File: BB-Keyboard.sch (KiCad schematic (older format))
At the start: 35 parts, among them SW1 SW_Q, SW10 SW_X, SW11 SW_0, SW12 SW_R, SW13 SW_F, SW14 SW_C, SW15 SW_T, SW16 SW_G, SW17 SW_V, SW18 SW_SPC, SW19 SW_Y, SW2 SW_A, SW20 SW_H, SW21 SW_B, SW22 SW_U, SW23 SW_J, SW24 SW_N, SW25 SW_I, SW26 SW_K, SW27 SW_M, SW28 SW_SYM, SW29 SW_O, SW3 SW_ALT, SW30 SW_L, SW31 SW_$, SW32 SW_RSHIFT, SW33 SW_P, SW34 SW_BK, SW35 SW_ENT, SW4 SW_W, SW5 SW_S, SW6 SW_Z, SW7 SW_LSHIFT, SW8 SW_E, SW9 SW_D

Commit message: Buses, labels, et al.
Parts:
- added D? (x35): D, symbol D
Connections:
- new net: D?.1 (K), SW1.2
- new net: D?.1 (K), SW4.2
- new net: D?.1 (K), SW8.2
- new net: D?.1 (K), SW12.2
- new net: D?.1 (K), SW15.2
- new net: D?.1 (K), SW19.2
- new net: D?.1 (K), SW22.2
- new net: D?.1 (K), SW25.2
- new net: D?.1 (K), SW29.2
- new net: D?.1 (K), SW33.2
- new net: D?.1 (K), SW2.2
- new net: D?.1 (K), SW5.2
- new net: D?.1 (K), SW9.2
- new net: D?.1 (K), SW13.2
- new net: D?.1 (K), SW16.2
- new net: D?.1 (K), SW20.2
- new net: D?.1 (K), SW23.2
- new net: D?.1 (K), SW26.2
- new net: D?.1 (K), SW30.2
- new net: D?.1 (K), SW34.2
- new net: D?.1 (K), SW3.2
- new net: D?.1 (K), SW6.2
- new net: D?.1 (K), SW10.2
- new net: D?.1 (K), SW14.2
- new net: D?.1 (K), SW17.2
- new net: D?.1 (K), SW21.2
- new net: D?.1 (K), SW24.2
- new net: D?.1 (K), SW27.2
- new net: D?.1 (K), SW31.2
- new net: D?.1 (K), SW35.2
- new net: D?.1 (K), SW7.2
- new net: D?.1 (K), SW11.2
- new net: D?.1 (K), SW18.1
- new net: D?.1 (K), SW28.2
- new net: D?.1 (K), SW32.2
- new net COL0: D?.2 (A)
- new net COL1: D?.2 (A)
- new net COL2: D?.2 (A)
- new net COL3: D?.2 (A)
- new net COL4: D?.2 (A)
- new net COL5: D?.2 (A)
- new net COL6: D?.2 (A)
- new net COL7: D?.2 (A)
- new net COL8: D?.2 (A)
- new net COL9: D?.2 (A)
- now unconnected: SW1.1, SW10.1, SW11.1, SW12.1, SW13.1, SW14.1, SW15.1, SW16.1, SW17.1, SW18.2, SW19.1, SW2.1, SW20.1, SW21.1, SW22.1, SW23.1, SW24.1, SW25.1, SW26.1, SW27.1, SW28.1, SW29.1, SW3.1, SW30.1, SW31.1, SW32.1, SW33.1, SW34.1, SW35.1, SW4.1, SW5.1, SW6.1, SW7.1, SW8.1, SW9.1
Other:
- moved on the sheet: SW1, SW10, SW11, SW12, SW13, SW14, SW15, SW16, SW17, SW18, SW19, SW2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

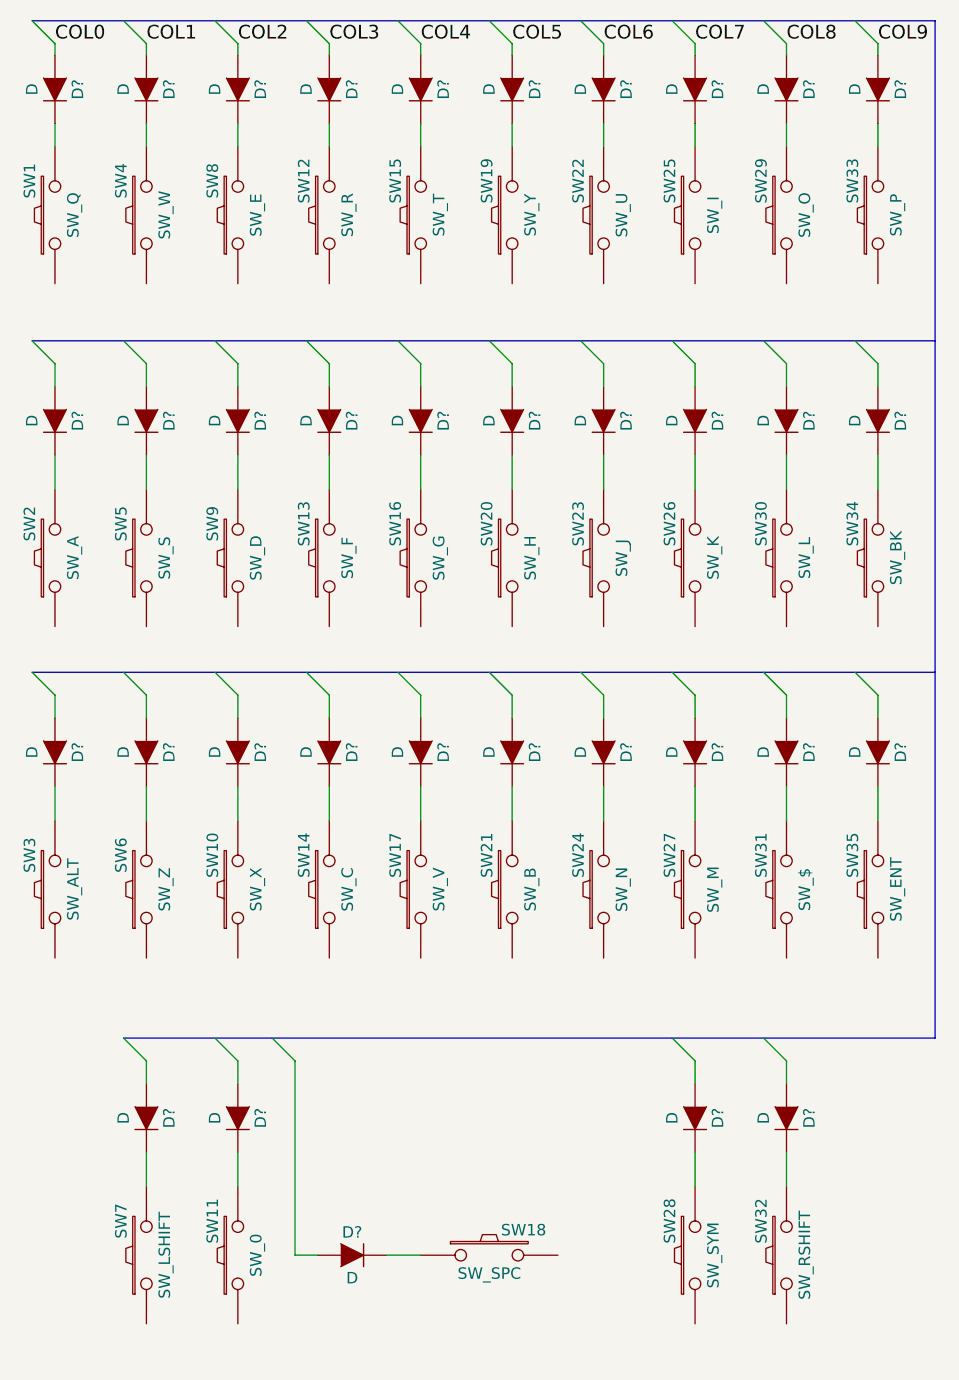
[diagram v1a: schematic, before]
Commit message: More labels and buses.
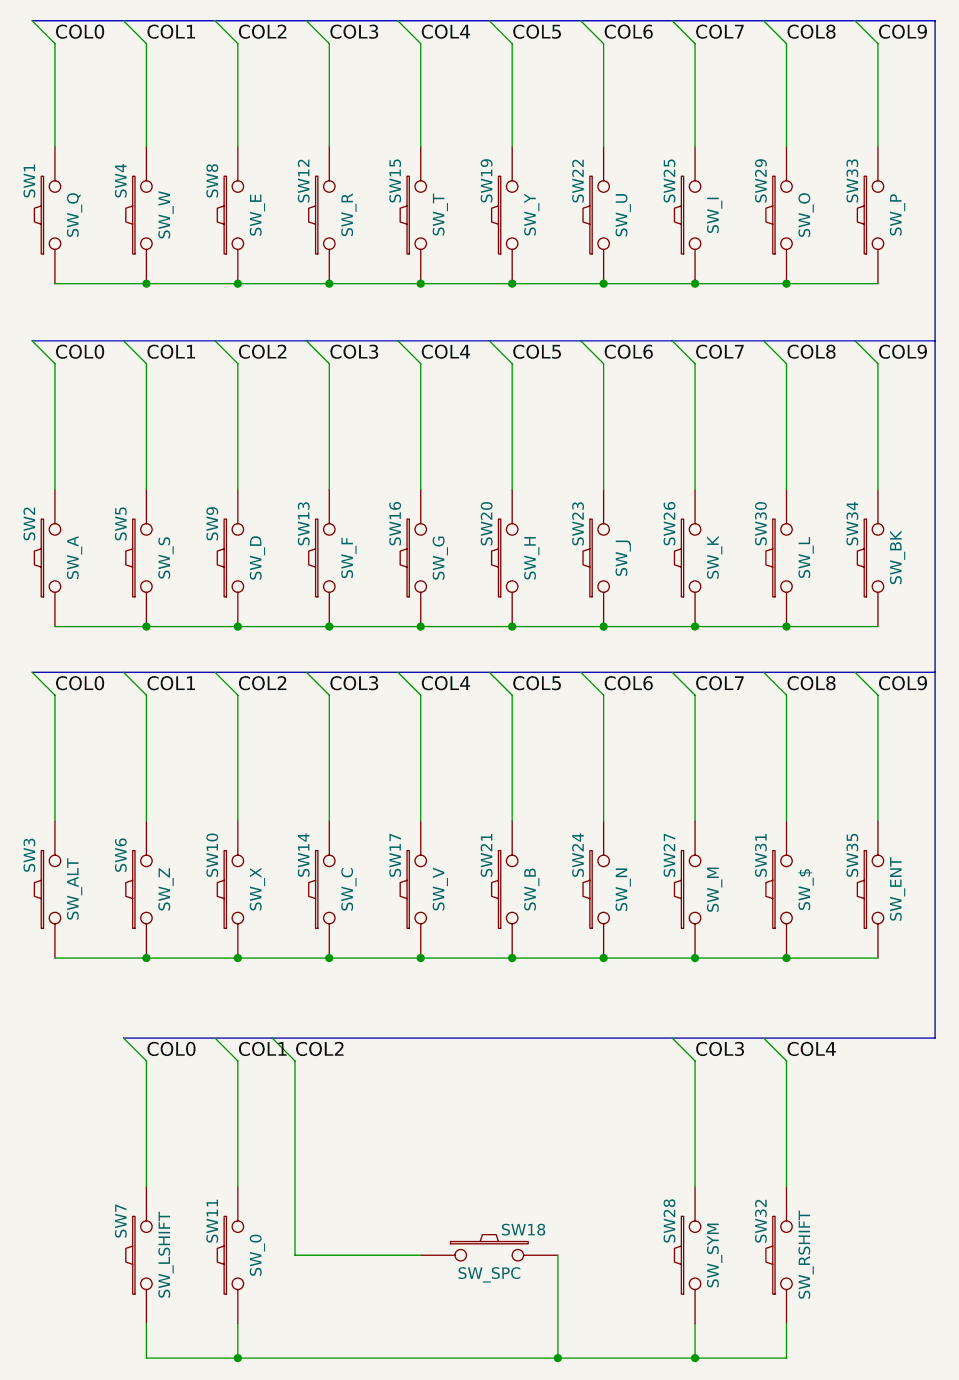
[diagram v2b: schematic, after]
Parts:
- removed D? (x35): D, symbol D
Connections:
- net COL0: now also SW1.2, SW2.2, SW3.2, SW7.2
- net COL1: now also SW11.2, SW4.2, SW5.2, SW6.2
- net COL2: now also SW10.2, SW18.1, SW8.2, SW9.2
- net COL3: now also SW12.2, SW13.2, SW14.2, SW28.2
- net COL4: now also SW15.2, SW16.2, SW17.2, SW32.2
- net COL5: now also SW19.2, SW20.2, SW21.2
- net COL6: now also SW22.2, SW23.2, SW24.2
- net COL7: now also SW25.2, SW26.2, SW27.2
- net COL8: now also SW29.2, SW30.2, SW31.2
- net COL9: now also SW33.2, SW34.2, SW35.2
- net at SW1.1: now also SW12.1, SW15.1, SW19.1, SW22.1, SW25.1, SW29.1, SW33.1, SW4.1, SW8.1
- net at SW2.1: now also SW13.1, SW16.1, SW20.1, SW23.1, SW26.1, SW30.1, SW34.1, SW5.1, SW9.1
- net at SW3.1: now also SW10.1, SW14.1, SW17.1, SW21.1, SW24.1, SW27.1, SW31.1, SW35.1, SW6.1
- net at SW7.1: now also SW11.1, SW18.2, SW28.1, SW32.1

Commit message: Finished schematic.
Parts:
- added C1: C_Small, symbol C_Small
- added P1: CONN_01X04, symbol CONN_01X04
- added R1, R2: 4.7k, symbol R
- added R3: 10k, symbol R
- added U1: TCA8418, symbol TCA8418
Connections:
- net COL0: now also U1.9 (COL0)
- net COL1: now also U1.10 (COL1)
- net COL2: now also U1.11 (COL2)
- net COL3: now also U1.12 (COL3)
- net COL4: now also U1.13 (COL4)
- net COL5: now also U1.14 (COL5)
- net COL6: now also U1.15 (COL6)
- net COL7: now also U1.16 (COL7)
- net COL8: now also U1.17 (COL8)
- net COL9: now also U1.18 (COL9)
- net ROW0: now reaches SW1.1, SW12.1, SW15.1, SW19.1, SW22.1, SW25.1, SW29.1, SW33.1, SW4.1, SW8.1
- net ROW0: now also U1.8 (ROW0)
- net ROW1: now reaches SW13.1, SW16.1, SW2.1, SW20.1, SW23.1, SW26.1, SW30.1, SW34.1, SW5.1, SW9.1
- net ROW1: now also U1.7 (ROW1)
- net ROW2: now reaches SW10.1, SW14.1, SW17.1, SW21.1, SW24.1, SW27.1, SW3.1, SW31.1, SW35.1, SW6.1
- net ROW2: now also U1.6 (ROW2)
- net ROW3: now reaches SW11.1, SW18.2, SW28.1, SW32.1, SW7.1
- net ROW3: now also U1.5 (ROW3)
- new net: R3.1, U1.1 (ROW7), U1.2 (ROW6), U1.20 (/RESET), U1.24 (/INT), U1.3 (ROW5), U1.4 (ROW4)
- new net +3V3: C1.1, P1.1 (P1), R1.1, R2.1, R3.2, U1.21 (VCC)
- new net GND: C1.2, P1.2 (P2), U1.19 (GND)
- new net SCL: P1.3 (P3), R1.2, U1.23 (SCL)
- new net SDA: P1.4 (P4), R2.2, U1.22 (SDA)

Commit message: WIP, component outline changed, but not reflected on PCB.
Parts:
- C1: footprint (none) -> Capacitors_SMD:C_1206_HandSoldering
- P1: footprint (none) -> Socket_Strips:Socket_Strip_Straight_1x04
- R1, R2, R3: footprint (none) -> Resistors_SMD:R_1206_HandSoldering
- SW1, SW10, SW11, SW12, SW13, SW14, SW15, SW16, SW17, SW18, SW19, SW2, SW20, SW21, SW22, SW23, SW24, SW25, SW26, SW27, SW28, SW29, SW3, SW30, SW31, SW32, SW33, SW34, SW35, SW4, SW5, SW6, SW7, SW8, SW9: footprint (none) -> TCA8418:SMD_Switch_4x3mm
- U1: footprint (none) -> TCA8418:TCA8418RTWR
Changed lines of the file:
@@
 F 0 "SW1" H 1300 1610 50  0000 C CNN
 F 1 "SW_Q" H 1150 1420 50  0000 C CNN
-F 2 "" H 1150 1500 50  0000 C CNN
+F 2 "TCA8418:SMD_Switch_4x3mm" H 1150 1500 50  0001 C CNN
 F 3 "" H 1150 1500 50  0000 C CNN
 	1    1150 1500
@@
 F 0 "SW4" H 1700 1610 50  0000 C CNN
 F 1 "SW_W" H 1550 1420 50  0000 C CNN
-F 2 "" H 1550 1500 50  0000 C CNN
+F 2 "TCA8418:SMD_Switch_4x3mm" H 1550 1500 50  0001 C CNN
 F 3 "" H 1550 1500 50  0000 C CNN
 	1    1550 1500
@@
 F 0 "SW12" H 2500 1610 50  0000 C CNN
 F 1 "SW_R" H 2350 1420 50  0000 C CNN
-F 2 "" H 2350 1500 50  0000 C CNN
+F 2 "TCA8418:SMD_Switch_4x3mm" H 2350 1500 50  0001 C CNN
 F 3 "" H 2350 1500 50  0000 C CNN
 	1    2350 1500
@@
 F 0 "SW15" H 2900 1610 50  0000 C CNN
 F 1 "SW_T" H 2750 1420 50  0000 C CNN
-F 2 "" H 2750 1500 50  0000 C CNN
+F 2 "TCA8418:SMD_Switch_4x3mm" H 2750 1500 50  0001 C CNN
 F 3 "" H 2750 1500 50  0000 C CNN
 	1    2750 1500
@@
 F 0 "SW19" H 3300 1610 50  0000 C CNN
 F 1 "SW_Y" H 3150 1420 50  0000 C CNN
-F 2 "" H 3150 1500 50  0000 C CNN
+F 2 "TCA8418:SMD_Switch_4x3mm" H 3150 1500 50  0001 C CNN
 F 3 "" H 3150 1500 50  0000 C CNN
 	1    3150 1500
@@
 F 0 "SW22" H 3700 1610 50  0000 C CNN
 F 1 "SW_U" H 3550 1420 50  0000 C CNN
-F 2 "" H 3550 1500 50  0000 C CNN
+F 2 "TCA8418:SMD_Switch_4x3mm" H 3550 1500 50  0001 C CNN
 F 3 "" H 3550 1500 50  0000 C CNN
 	1    3550 1500
@@
 F 0 "SW25" H 4100 1610 50  0000 C CNN
 F 1 "SW_I" H 3950 1420 50  0000 C CNN
-F 2 "" H 3950 1500 50  0000 C CNN
+F 2 "TCA8418:SMD_Switch_4x3mm" H 3950 1500 50  0001 C CNN
 F 3 "" H 3950 1500 50  0000 C CNN
 	1    3950 1500
@@
 F 0 "SW29" H 4500 1610 50  0000 C CNN
 F 1 "SW_O" H 4350 1420 50  0000 C CNN
-F 2 "" H 4350 1500 50  0000 C CNN
+F 2 "TCA8418:SMD_Switch_4x3mm" H 4350 1500 50  0001 C CNN
 F 3 "" H 4350 1500 50  0000 C CNN
 	1    4350 1500
@@
 F 0 "SW33" H 4900 1610 50  0000 C CNN
 F 1 "SW_P" H 4750 1420 50  0000 C CNN
-F 2 "" H 4750 1500 50  0000 C CNN
+F 2 "TCA8418:SMD_Switch_4x3mm" H 4750 1500 50  0001 C CNN
 F 3 "" H 4750 1500 50  0000 C CNN
 	1    4750 1500
@@
 F 0 "SW2" H 1300 3110 50  0000 C CNN
 F 1 "SW_A" H 1150 2920 50  0000 C CNN
-F 2 "" H 1150 3000 50  0000 C CNN
+F 2 "TCA8418:SMD_Switch_4x3mm" H 1150 3000 50  0001 C CNN
 F 3 "" H 1150 3000 50  0000 C CNN
 	1    1150 3000
@@
 F 0 "SW5" H 1700 3110 50  0000 C CNN
 F 1 "SW_S" H 1550 2920 50  0000 C CNN
-F 2 "" H 1550 3000 50  0000 C CNN
+F 2 "TCA8418:SMD_Switch_4x3mm" H 1550 3000 50  0001 C CNN
 F 3 "" H 1550 3000 50  0000 C CNN
 	1    1550 3000
@@
 F 0 "SW9" H 2100 3110 50  0000 C CNN
 F 1 "SW_D" H 1950 2920 50  0000 C CNN
-F 2 "" H 1950 3000 50  0000 C CNN
+F 2 "TCA8418:SMD_Switch_4x3mm" H 1950 3000 50  0001 C CNN
 F 3 "" H 1950 3000 50  0000 C CNN
 	1    1950 3000
@@
 F 0 "SW13" H 2500 3110 50  0000 C CNN
 F 1 "SW_F" H 2350 2920 50  0000 C CNN
-F 2 "" H 2350 3000 50  0000 C CNN
+F 2 "TCA8418:SMD_Switch_4x3mm" H 2350 3000 50  0001 C CNN
 F 3 "" H 2350 3000 50  0000 C CNN
 	1    2350 3000
@@
 F 0 "SW16" H 2900 3110 50  0000 C CNN
 F 1 "SW_G" H 2750 2920 50  0000 C CNN
-F 2 "" H 2750 3000 50  0000 C CNN
+F 2 "TCA8418:SMD_Switch_4x3mm" H 2750 3000 50  0001 C CNN
 F 3 "" H 2750 3000 50  0000 C CNN
 	1    2750 3000
@@
 F 0 "SW20" H 3300 3110 50  0000 C CNN
 F 1 "SW_H" H 3150 2920 50  0000 C CNN
-F 2 "" H 3150 3000 50  0000 C CNN
+F 2 "TCA8418:SMD_Switch_4x3mm" H 3150 3000 50  0001 C CNN
 F 3 "" H 3150 3000 50  0000 C CNN
 	1    3150 3000
@@
 F 0 "SW23" H 3700 3110 50  0000 C CNN
 F 1 "SW_J" H 3550 2920 50  0000 C CNN
-F 2 "" H 3550 3000 50  0000 C CNN
+F 2 "TCA8418:SMD_Switch_4x3mm" H 3550 3000 50  0001 C CNN
 F 3 "" H 3550 3000 50  0000 C CNN
 	1    3550 3000
@@
 F 0 "SW26" H 4100 3110 50  0000 C CNN
 F 1 "SW_K" H 3950 2920 50  0000 C CNN
-F 2 "" H 3950 3000 50  0000 C CNN
+F 2 "TCA8418:SMD_Switch_4x3mm" H 3950 3000 50  0001 C CNN
 F 3 "" H 3950 3000 50  0000 C CNN
 	1    3950 3000
@@
 F 0 "SW30" H 4500 3110 50  0000 C CNN
 F 1 "SW_L" H 4350 2920 50  0000 C CNN
-F 2 "" H 4350 3000 50  0000 C CNN
+F 2 "TCA8418:SMD_Switch_4x3mm" H 4350 3000 50  0001 C CNN
 F 3 "" H 4350 3000 50  0000 C CNN
 	1    4350 3000
@@
 F 0 "SW34" H 4900 3110 50  0000 C CNN
 F 1 "SW_BK" H 4750 2920 50  0000 C CNN
-F 2 "" H 4750 3000 50  0000 C CNN
+F 2 "TCA8418:SMD_Switch_4x3mm" H 4750 3000 50  0001 C CNN
 F 3 "" H 4750 3000 50  0000 C CNN
 	1    4750 3000
@@
 F 0 "SW3" H 1300 4560 50  0000 C CNN
 F 1 "SW_ALT" H 1150 4370 50  0000 C CNN
-F 2 "" H 1150 4450 50  0000 C CNN
+F 2 "TCA8418:SMD_Switch_4x3mm" H 1150 4450 50  0001 C CNN
 F 3 "" H 1150 4450 50  0000 C CNN
 	1    1150 4450
@@
 F 0 "SW6" H 1700 4560 50  0000 C CNN
 F 1 "SW_Z" H 1550 4370 50  0000 C CNN
-F 2 "" H 1550 4450 50  0000 C CNN
+F 2 "TCA8418:SMD_Switch_4x3mm" H 1550 4450 50  0001 C CNN
 F 3 "" H 1550 4450 50  0000 C CNN
 	1    1550 4450
@@
 F 0 "SW10" H 2100 4560 50  0000 C CNN
 F 1 "SW_X" H 1950 4370 50  0000 C CNN
-F 2 "" H 1950 4450 50  0000 C CNN
+F 2 "TCA8418:SMD_Switch_4x3mm" H 1950 4450 50  0001 C CNN
 F 3 "" H 1950 4450 50  0000 C CNN
 	1    1950 4450
@@
 F 0 "SW14" H 2500 4560 50  0000 C CNN
 F 1 "SW_C" H 2350 4370 50  0000 C CNN
-F 2 "" H 2350 4450 50  0000 C CNN
+F 2 "TCA8418:SMD_Switch_4x3mm" H 2350 4450 50  0001 C CNN
 F 3 "" H 2350 4450 50  0000 C CNN
 	1    2350 4450
@@
 F 0 "SW17" H 2900 4560 50  0000 C CNN
 F 1 "SW_V" H 2750 4370 50  0000 C CNN
-F 2 "" H 2750 4450 50  0000 C CNN
+F 2 "TCA8418:SMD_Switch_4x3mm" H 2750 4450 50  0001 C CNN
 F 3 "" H 2750 4450 50  0000 C CNN
 	1    2750 4450
@@
 F 0 "SW21" H 3300 4560 50  0000 C CNN
 F 1 "SW_B" H 3150 4370 50  0000 C CNN
-F 2 "" H 3150 4450 50  0000 C CNN
+F 2 "TCA8418:SMD_Switch_4x3mm" H 3150 4450 50  0001 C CNN
 F 3 "" H 3150 4450 50  0000 C CNN
 	1    3150 4450
@@
 F 0 "SW24" H 3700 4560 50  0000 C CNN
 F 1 "SW_N" H 3550 4370 50  0000 C CNN
-F 2 "" H 3550 4450 50  0000 C CNN
+F 2 "TCA8418:SMD_Switch_4x3mm" H 3550 4450 50  0001 C CNN
 F 3 "" H 3550 4450 50  0000 C CNN
 	1    3550 4450
@@
 F 0 "SW27" H 4100 4560 50  0000 C CNN
 F 1 "SW_M" H 3950 4370 50  0000 C CNN
-F 2 "" H 3950 4450 50  0000 C CNN
+F 2 "TCA8418:SMD_Switch_4x3mm" H 3950 4450 50  0001 C CNN
 F 3 "" H 3950 4450 50  0000 C CNN
 	1    3950 4450
@@
 F 0 "SW31" H 4500 4560 50  0000 C CNN
 F 1 "SW_$" H 4350 4370 50  0000 C CNN
-F 2 "" H 4350 4450 50  0000 C CNN
+F 2 "TCA8418:SMD_Switch_4x3mm" H 4350 4450 50  0001 C CNN
 F 3 "" H 4350 4450 50  0000 C CNN
 	1    4350 4450
@@
 F 0 "SW35" H 4900 4560 50  0000 C CNN
 F 1 "SW_ENT" H 4750 4370 50  0000 C CNN
-F 2 "" H 4750 4450 50  0000 C CNN
+F 2 "TCA8418:SMD_Switch_4x3mm" H 4750 4450 50  0001 C CNN
 F 3 "" H 4750 4450 50  0000 C CNN
 	1    4750 4450
@@
 F 0 "SW7" H 1700 6160 50  0000 C CNN
 F 1 "SW_LSHIFT" H 1550 5970 50  0000 C CNN
-F 2 "" H 1550 6050 50  0000 C CNN
+F 2 "TCA8418:SMD_Switch_4x3mm" H 1550 6050 50  0001 C CNN
 F 3 "" H 1550 6050 50  0000 C CNN
 	1    1550 6050
@@
 F 0 "SW11" H 2100 6160 50  0000 C CNN
 F 1 "SW_0" H 1950 5970 50  0000 C CNN
-F 2 "" H 1950 6050 50  0000 C CNN
+F 2 "TCA8418:SMD_Switch_4x3mm" H 1950 6050 50  0001 C CNN
 F 3 "" H 1950 6050 50  0000 C CNN
 	1    1950 6050
@@
 F 0 "SW18" H 3200 6160 50  0000 C CNN
 F 1 "SW_SPC" H 3050 5970 50  0000 C CNN
-F 2 "" H 3050 6050 50  0000 C CNN
+F 2 "TCA8418:SMD_Switch_4x3mm" H 3050 6050 50  0001 C CNN
 F 3 "" H 3050 6050 50  0000 C CNN
 	1    3050 6050
@@
 F 0 "SW28" H 4100 6160 50  0000 C CNN
 F 1 "SW_SYM" H 3950 5970 50  0000 C CNN
-F 2 "" H 3950 6050 50  0000 C CNN
+F 2 "TCA8418:SMD_Switch_4x3mm" H 3950 6050 50  0001 C CNN
 F 3 "" H 3950 6050 50  0000 C CNN
 	1    3950 6050
@@
 F 0 "SW32" H 4500 6160 50  0000 C CNN
 F 1 "SW_RSHIFT" H 4350 5970 50  0000 C CNN
-F 2 "" H 4350 6050 50  0000 C CNN
+F 2 "TCA8418:SMD_Switch_4x3mm" H 4350 6050 50  0001 C CNN
 F 3 "" H 4350 6050 50  0000 C CNN
 	1    4350 6050
@@
 F 0 "SW8" H 2100 1610 50  0000 C CNN
 F 1 "SW_E" H 1950 1420 50  0000 C CNN
-F 2 "" H 1950 1500 50  0000 C CNN
+F 2 "TCA8418:SMD_Switch_4x3mm" H 1950 1500 50  0001 C CNN
 F 3 "" H 1950 1500 50  0000 C CNN
 	1    1950 1500
@@
 F 0 "R3" V 7880 1700 50  0000 C CNN
 F 1 "10k" V 7800 1700 50  0000 C CNN
-F 2 "" V 7730 1700 50  0000 C CNN
+F 2 "Resistors_SMD:R_1206_HandSoldering" V 7730 1700 50  0001 C CNN
 F 3 "" H 7800 1700 50  0000 C CNN
 	1    7800 1700
@@
 F 0 "P1" H 9950 5800 50  0000 C CNN
 F 1 "CONN_01X04" V 10050 5550 50  0000 C CNN
-F 2 "" H 9950 5550 50  0000 C CNN
+F 2 "Socket_Strips:Socket_Strip_Straight_1x04" H 9950 5550 50  0001 C CNN
 F 3 "" H 9950 5550 50  0000 C CNN
 	1    9950 5550
@@
 F 0 "C1" H 7910 2420 50  0000 L CNN
 F 1 "C_Small" H 7910 2270 50  0000 L CNN
-F 2 "" H 7900 2350 50  0000 C CNN
+F 2 "Capacitors_SMD:C_1206_HandSoldering" H 7900 2350 50  0001 C CNN
 F 3 "" H 7900 2350 50  0000 C CNN
 	1    7900 2350
@@
 F 0 "R2" V 7580 1350 50  0000 C CNN
 F 1 "4.7k" V 7500 1350 50  0000 C CNN
-F 2 "" V 7430 1350 50  0000 C CNN
+F 2 "Resistors_SMD:R_1206_HandSoldering" V 7430 1350 50  0001 C CNN
 F 3 "" H 7500 1350 50  0000 C CNN
 	1    7500 1350
@@
 F 0 "R1" V 7280 1350 50  0000 C CNN
 F 1 "4.7k" V 7200 1350 50  0000 C CNN
-F 2 "" V 7130 1350 50  0000 C CNN
+F 2 "Resistors_SMD:R_1206_HandSoldering" V 7130 1350 50  0001 C CNN
 F 3 "" H 7200 1350 50  0000 C CNN
 	1    7200 1350
@@
 F 0 "U1" H 7650 3650 60  0000 C CNN
 F 1 "TCA8418" H 7650 3750 60  0000 C CNN
-F 2 "" H 7650 3650 60  0000 C CNN
+F 2 "TCA8418:TCA8418RTWR" H 7650 3650 60  0001 C CNN
 F 3 "" H 7650 3650 60  0000 C CNN
 	1    7650 3650
